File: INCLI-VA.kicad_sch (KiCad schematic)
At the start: 4 parts

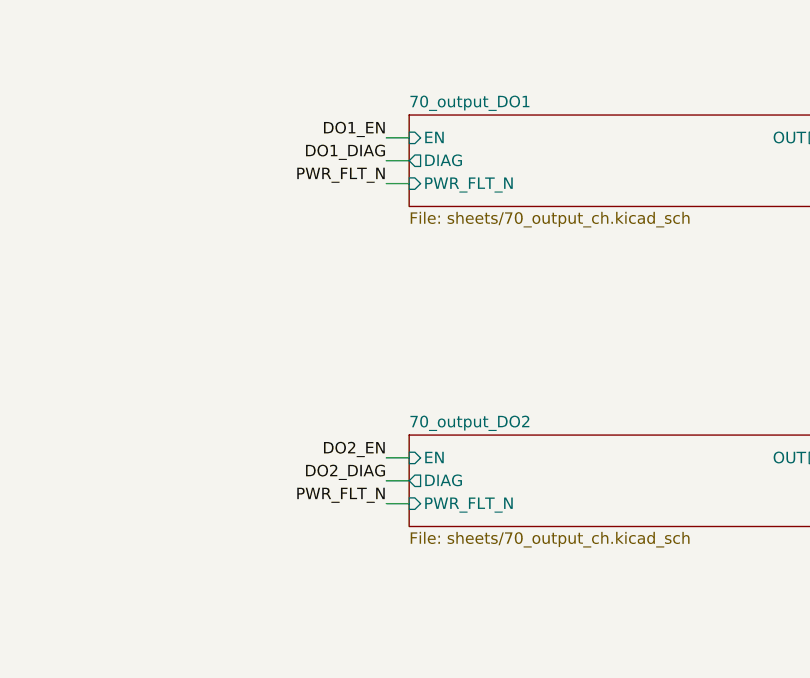
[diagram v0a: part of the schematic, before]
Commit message: [Claude Code] 70_output: retira latch de sobrecorriente y R701/R751; borra propuesta 120x80
- 70_output_ch (DO1/DO2): fuera Q702/Q703, D702, R704-R707, C701 y R701
  (y equivalentes 75x). Fuente de Q701 directo a GND_VEH. PWR_FLT_N deja de
  entrar a la hoja 70 (pin jerarquico y conexiones de la raiz retirados).
  Se conserva el diagnostico (DNP en PROTO).
- ERC 0 errores / 1 aviso conocido. Paridad con la propuesta 100x100:
  22 diferencias esperadas, pendiente Update PCB from Schematic.
- docs/layout: se borra la propuesta 120x80 (recuperable de aa0a41b).

Co-Authored-By: Claude Opus 5.5 <noreply@anthropic.com>
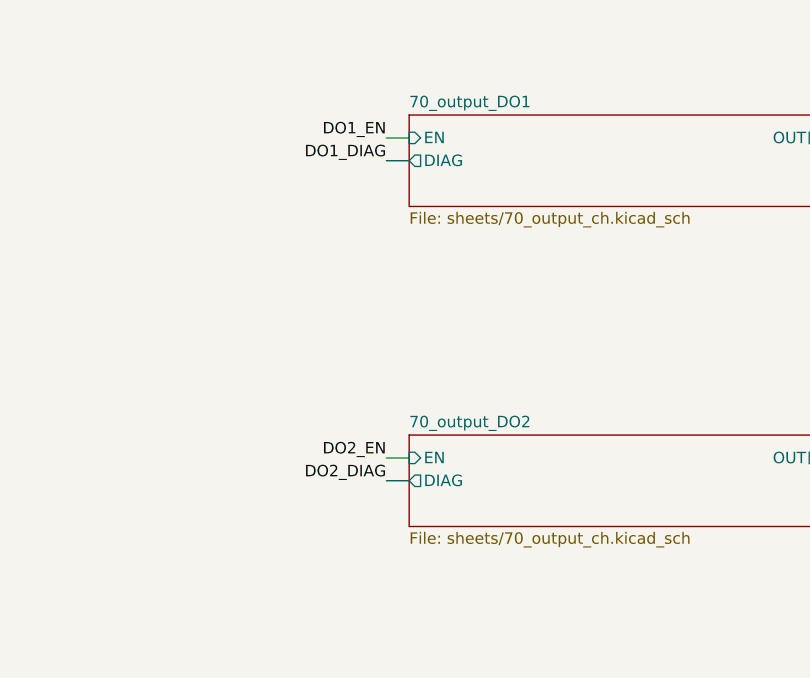
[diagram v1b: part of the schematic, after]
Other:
- sheet 70_output_DO1 ports: added none; removed PWR_FLT_N
- sheet 70_output_DO2 ports: added none; removed PWR_FLT_N
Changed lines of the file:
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@@
-	(wire
-		(pts
-			(xy 297.18 83.82) (xy 294.64 83.82)
-		)
-		(stroke
-			(width 0)
-			(type default)
-		)
-	)
 	(wire
 		(pts
@@
 		(pts
 			(xy 342.9 78.74) (xy 345.44 78.74)
-		)
-		(stroke
-			(width 0)
-			(type default)
-		)
-	)
-	(wire
-		(pts
-			(xy 297.18 48.26) (xy 294.64 48.26)
 		)
 		(stroke
@@
 		)
 	)
-	(label "PWR_FLT_N"
-		(at 294.64 48.26 180)
-		(effects
-			(font
-				(size 1.27 1.27)
-			)
-			(justify right bottom)
-		)
-	)
 	(label "SPI_MOSI"
 		(at 294.64 129.54 180)
@@
 	(label "DO1_DIAG"
 		(at 294.64 45.72 180)
-		(effects
-			(font
-				(size 1.27 1.27)
-			)
-			(justify right bottom)
-		)
-	)
-	(label "PWR_FLT_N"
-		(at 294.64 83.82 180)
 		(effects
 			(font
@@
 			)
 		)
-		(pin "PWR_FLT_N" input
-			(at 297.18 83.82 180)
-			(effects
-				(font
-					(size 1.27 1.27)
-				)
-				(justify left)
-			)
-		)
 		(instances
 			(project "INCLI-VA"
@@
 			)
 		)
-		(pin "PWR_FLT_N" input
-			(at 297.18 48.26 180)
-			(effects
-				(font
-					(size 1.27 1.27)
-				)
-				(justify left)
-			)
-		)

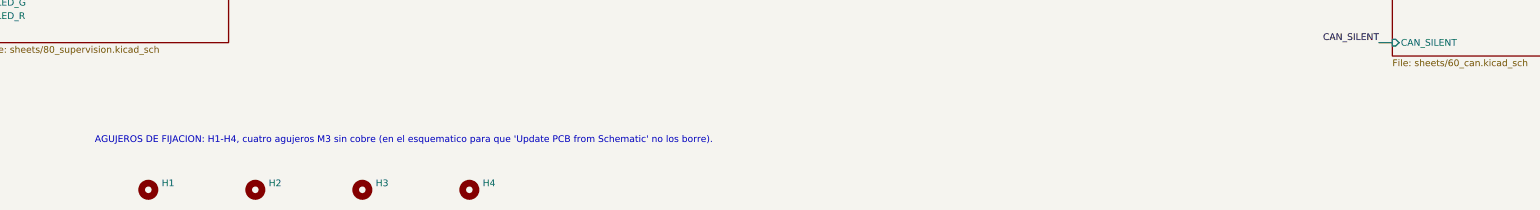
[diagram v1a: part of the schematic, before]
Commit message: [Claude Code] PCB: reacomodo por bloques segun docs/reference, H5 intermedio y barrera CAN
- Entrada -> proteccion -> bulk -> buck en la esquina superior izquierda;
  pasivos de U101 junto a sus pines; C107/C106 junto a la salida de L101.
- CAN: U601 sobre la barrera con el lado aislado hacia J1; rule area
  BARRERA_CAN en F.Cu/B.Cu (solo U601 la cruza; FB602 es aislado-aislado).
  DRU: pin 17 de U601 (AUXOUT NC) cuenta como dominio aislado.
- DO1/DO2 bajo su pin de J2 (antes cruzados). USB-C al borde derecho con
  U402 en linea; SW401 junto al EN; C402/C401 en los pines de 3V3.
- H5 (M3 NPTH) en esquematico y PCB junto a U501/U502, a 18 mm del eje ROT.
- DRC 0 errores / 1 aviso U401 / paridad 0; ERC 0 / 1 aviso conocido.
- Incluye docs/reference (fotos UG-230 e INCLIMAX) y scripts/layout_bloques.

Co-Authored-By: Claude Opus 5.5 <noreply@anthropic.com>
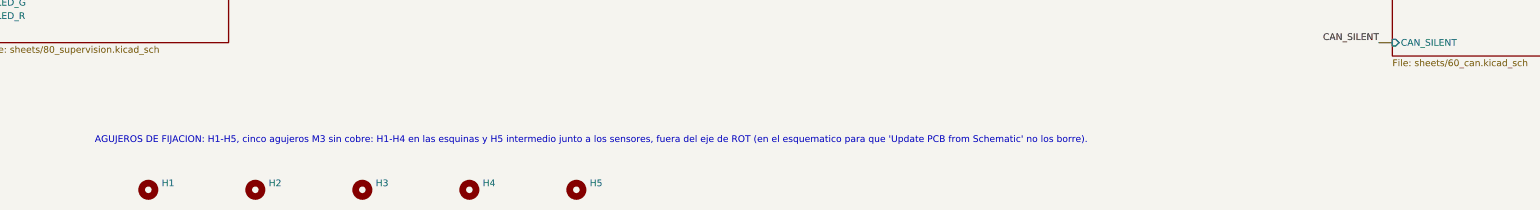
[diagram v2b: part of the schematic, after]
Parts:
- added H5: MountingHole_M3, MountingHole:MountingHole_3.2mm_M3, symbol Mechanical:MountingHole
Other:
- note added: "AGUJEROS DE FIJACION: H1-H5, cinco agujeros M3 sin cobre: H1-H4 en las esquinas y H5 intermedio junto a los sensores, fuera del eje de ROT (en el esquematico para que 'Update PCB from Schematic' no los borre)."
- note removed: "AGUJEROS DE FIJACION: H1-H4, cuatro agujeros M3 sin cobre (en el esquematico para que 'Update PCB from Schematic' no los borre)."
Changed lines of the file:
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@@
 		)
 	)
-	(text "AGUJEROS DE FIJACION: H1-H4, cuatro agujeros M3 sin cobre (en el esquematico para que 'Update PCB from Schematic' no los borre)."
+	(symbol
+		(lib_id "Mechanical:MountingHole")
+		(at 142.24 256.54 0)
+		(unit 1)
+		(body_style 1)
+		(exclude_from_sim no)
+		(in_bom no)
+		(on_board yes)
+		(in_pos_files yes)
+		(dnp no)
+		(property "Reference" "H5"
+			(at 144.78 255.27 0)
+			(show_name no)
+			(do_not_autoplace no)
+			(effects
+				(font
+					(size 1.27 1.27)
+				)
+				(justify left)
+			)
+		)
+		(property "Value" "MountingHole_M3"
+			(at 144.78 257.81 0)
+			(show_name no)
+			(do_not_autoplace no)
+			(effects
+				(hide yes)
+				(font
+					(size 1.27 1.27)
+				)
+				(justify left)
+			)
+		)
+		(property "Footprint" "MountingHole:MountingHole_3.2mm_M3"
+			(at 142.24 256.54 0)
+			(hide yes)
+			(show_name no)
+			(do_not_autoplace no)
+			(effects
+				(font
+					(size 1.27 1.27)
+				)
+			)
+		)
+		(property "Datasheet" "https://www.kicad.org/libraries/"
+			(at 142.24 256.54 0)
+			(hide yes)
+			(show_name no)
+			(do_not_autoplace no)
+			(effects
+				(font
+					(size 1.27 1.27)
+				)
+			)
+		)
+		(property "Description" ""
+			(at 142.24 256.54 0)
+			(hide yes)
+			(show_name no)
+			(do_not_autoplace no)
+			(effects
+				(font
+					(size 1.27 1.27)
+				)
+			)
+		)
+		(property "MPN" "N/A (agujero NPTH)"
+			(at 142.24 256.54 0)
+			(hide yes)
+			(show_name no)
+			(do_not_autoplace no)
+			(effects
+				(font
+					(size 1.27 1.27)
+				)
+			)
+		)
+		(property "Manufacturer" "N/A"
+			(at 142.24 256.54 0)
+			(hide yes)
+			(show_name no)
+			(do_not_autoplace no)
+			(effects
+				(font
+					(size 1.27 1.27)
+				)
+			)
+		)
+		(property "DNP" ""
+			(at 142.24 256.54 0)
+			(hide yes)
+			(show_name no)
+			(do_not_autoplace no)
+			(effects
+				(font
+					(size 1.27 1.27)
+				)
+			)
+		)
+		(property "Notes" "Agujero de fijacion M3 (3.2 mm), SIN cobre (NPTH): separador plastico, no puentea dominios. Courtyard de 6.9 mm para arandela/cabeza. Posicion: la define el layout (ver docs/LAYOUT_NOTES.md)."
+			(at 142.24 256.54 0)
+			(hide yes)
+			(show_name no)
+			(do_not_autoplace no)
+			(effects
+				(font
+					(size 1.27 1.27)
+				)
+			)
+		)
+		(instances
+			(project "INCLI-VA"
+				(path "/7fd92c2b-4254-4d73-93ba-bfde861bede3"
+					(reference "H5")
+					(unit 1)
+				)
+			)
+		)
+	)
+	(text "AGUJEROS DE FIJACION: H1-H5, cinco agujeros M3 sin cobre: H1-H4 en las esquinas y H5 intermedio junto a los sensores, fuera del eje de ROT (en el esquematico para que 'Update PCB from Schematic' no los borre)."
 		(exclude_from_sim no)
 		(at 50.8 246.38 0)
